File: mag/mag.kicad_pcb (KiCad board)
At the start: 4 copper layers, 68 x 41 mm, 67 parts, among them K1 кнопка_FSMSM, K2 кнопка_FSMSM, K3 кнопка_FSMSM, X1 Клеммник_х2

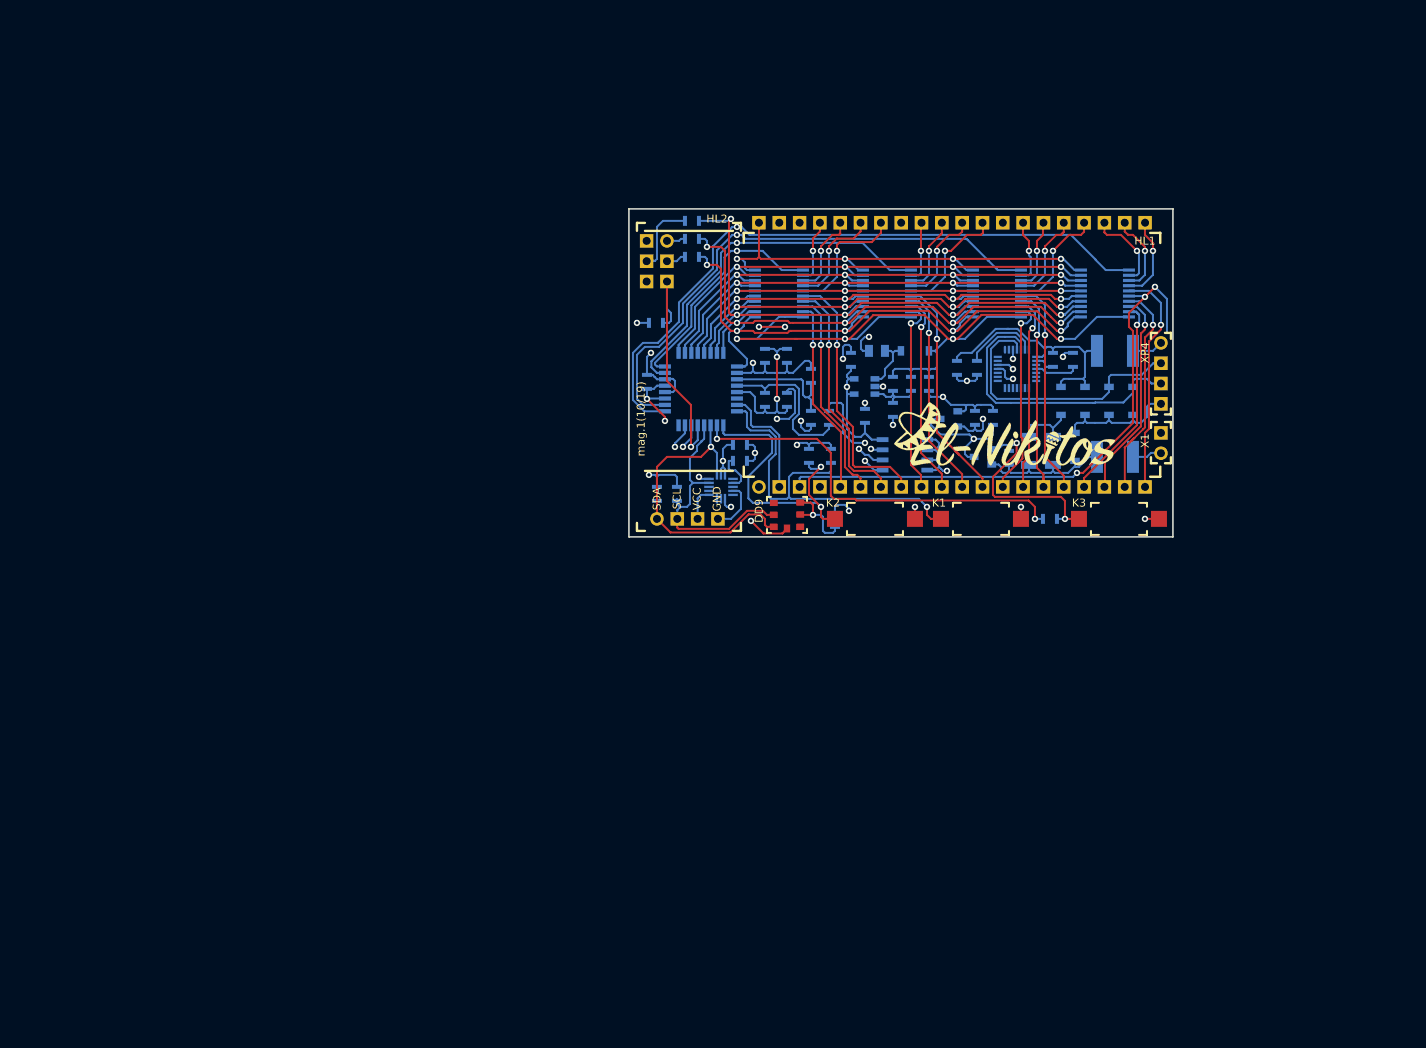
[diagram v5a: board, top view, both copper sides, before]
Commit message: инициирован переезд на ESP32
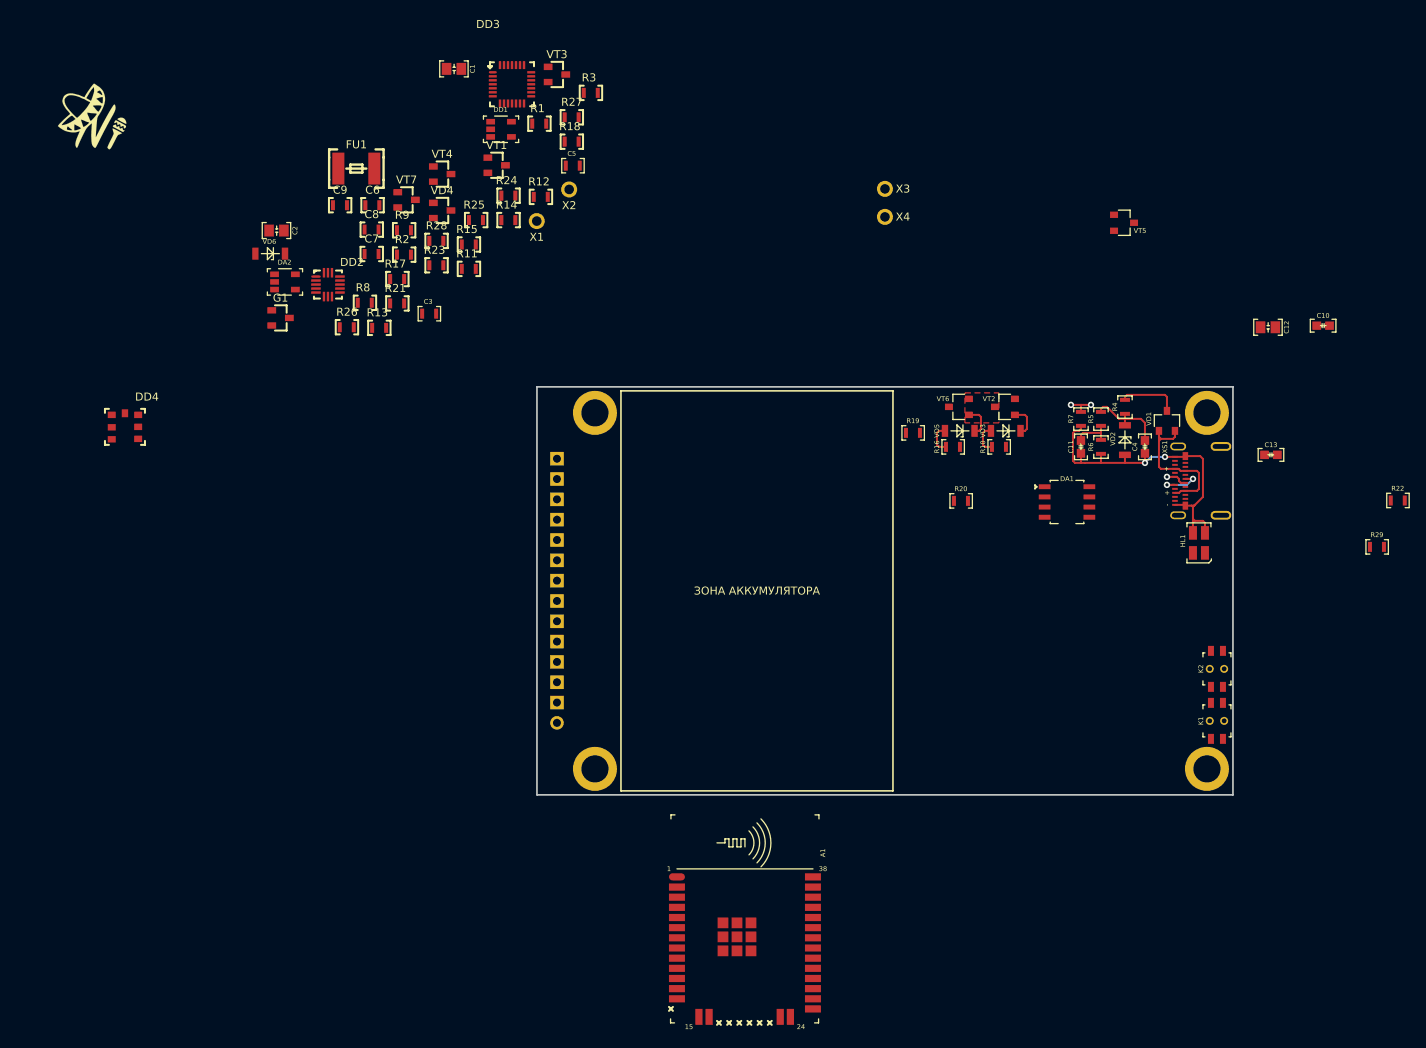
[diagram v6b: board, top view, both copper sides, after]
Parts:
- removed C14, C15: Конденсатор_керамический, N_RLC:Конденсатор_SMD_0603
- removed DD5: D-triger_74VHC573MTC, N_DD:SSOP-20
- removed DD6: LIS3DH, N_DD:акселерометр_LIS3DH
- removed DD7: Память_eeprom_AT24C512C, N_DD:SO-8
- removed DD8: Преобразователь_CP2102(USB-UART), N_DD:Микросхема_CP2102
- removed DD9: Датчик_bmp180, N_DD:BMP180
- removed FU2: Предохранитель_MF-MSMF010, N_RLC:Предохранитель_SMD_1812
- removed G***: LOGO, N_ICO:el-nikitos_29x10
- removed G***: LOGO, N_ICO:instagram_3x3
- removed G***: LOGO, N_ICO:skyer_19x4
- removed G2: Микросхема_DCDC_step_UP_TPS61040, N_G:Преобразователь_LM2703_SOT-23-5
- removed K3: кнопка_FSMSM, N_X:Кнопка_FSMSM
- removed L1: Чип-индуктивность, N_RLC:Чип-индуктивность_SMD_0805
- removed XP3: Вилка_PLD6_ПРОГ, N_X:Вилка_PLD6_вертикальная
- removed XP4: USB_female, N_X:Вилка_PLS4_вертикальная
- added A1: модуль_esp32_wroom_32_SMD_noSD, N_A:ESP32_WROOM32_pnp_noSD, F.Cu at (116.0, 132.8)
- added D1: LOGO, N_ICO:ni_10x10, F.Cu at (35.0, 29.2)
- added DA1: ОУ_LM358DT, MOTOR_IMPORT_OTK:SO-8, F.Cu at (153.5, 75.0)
- added DA2: ОУ_LMV321ILT, N_G:SOT-23-5_pnp, F.Cu at (58.5, 49.4)
- added R21: Резистор_0,065Вт, N_RLC:Резистор_SMD_0603_0,065_Вт, F.Cu at (72.5, 52.1)
- added R22: Резистор*1кОм*0603, N_RLC:Резистор_SMD_0603_0,065_Вт_pnp, F.Cu at (197.6, 76.7)
- added R23: Резистор_0,065Вт, N_RLC:Резистор_SMD_0603_0,065_Вт, F.Cu at (77.4, 47.3)
- added R24: Резистор_0,065Вт, N_RLC:Резистор_SMD_0603_0,065_Вт, F.Cu at (86.4, 38.6)
- added R25: Резистор_0,065Вт, N_RLC:Резистор_SMD_0603_0,065_Вт, F.Cu at (82.4, 41.6)
- added R26: Резистор_0,065Вт, N_RLC:Конденсатор_SMD_0603, F.Cu at (65.3, 55.0)
- added R27: Резистор_0,065Вт, N_RLC:Конденсатор_SMD_0603, F.Cu at (93.5, 28.8)
- added R28: Резистор_0,065Вт, N_RLC:Конденсатор_SMD_0603, F.Cu at (76.5, 44.2)
- added R29: Резистор*1кОм*0603, N_RLC:Резистор_SMD_0603_0,065_Вт_pnp, F.Cu at (195.0, 82.5)
- added VT2: Транзистор*pnp*0,5А*45В*SOT23, N_VD_HL:Корпус_КТ-46, F.Cu at (148.5, 65.0)
- added VT3: Транзистор_полевой_P-канал(IRLML2246TRPBF), N_VD_HL:Транзистор_IRLML6344TR_SOT-23, F.Cu at (92.5, 23.4)
- added VT4: Транзистор_полевой_N-IRLML6344TR, N_VD_HL:Транзистор_IRLML6344TR_SOT-23, F.Cu at (78.2, 35.9)
- added VT5: Транзистор*npn*0,5А*45В*SOT23, N_VD_HL:Корпус_КТ-46, F.Cu at (163.4, 42.0)
- added VT6: Транзистор*pnp*0,5А*45В*SOT23, N_VD_HL:Корпус_КТ-46, F.Cu at (142.8, 65.0)
- added VT7: Транзистор_полевой_P-канал(IRLML2246TRPBF), N_VD_HL:Транзистор_IRLML6344TR_SOT-23, F.Cu at (73.7, 39.1)
- added X2: отверстие_под_пайку, N_X:ОтверстиеD1.2, F.Cu at (94.0, 37.8)
- added X3: отверстие_под_пайку, N_X:ОтверстиеD1.2, F.Cu at (133.5, 37.8)
- added X4: отверстие_под_пайку, N_X:ОтверстиеD1.2, F.Cu at (133.5, 41.2)
- added XS1: UBS-type-C-105450-0101&упрощенная, N_X:usb-type-c, F.Cu at (169.8, 77.2)
- C1, C2: footprint N_RLC:Конденсатор_SMD_0603 -> N_RLC:Конденсатор_SMD_IEC_0805; moved to F.Cu
- C10, C11, C13, C4: value Конденсатор_керамический -> Конденсатор*0,1мкФ*25В*0603; footprint N_RLC:Конденсатор_SMD_0603 -> N_RLC:Конденсатор_SMD_IEC_0603; moved to F.Cu
- C12: value Конденсатор_керамический -> Конденсатор*10мкФ*16В*0805; footprint N_RLC:Конденсатор_SMD_0603 -> N_RLC:Конденсатор_SMD_IEC_0805; moved to F.Cu
- C3, C5: footprint N_RLC:Конденсатор_SMD_0603 -> N_RLC:Конденсатор_SMD_0603_pnp; moved to F.Cu
- C6, C7, C8, C9, VT1: moved to F.Cu
- DD1: value ATmega328 -> Микросхема_заряда_MCP73831T-2ACI_OT; footprint N_DD:микросхема_ATMEGA-8-161AU -> N_G:SOT-23-5_pnp; moved to F.Cu
- DD2: value D-triger_74VHC573MTC -> LIS3DH; footprint N_DD:SSOP-20 -> N_DD:акселерометр_LIS3DH; moved to F.Cu
- DD3: value D-triger_74VHC573MTC -> Преобразователь_CP2102(USB-UART); footprint N_DD:SSOP-20 -> N_DD:Микросхема_CP2102; moved to F.Cu
- DD4: value D-triger_74VHC573MTC -> Датчик_bmp180; footprint N_DD:SSOP-20 -> N_DD:BMP180; moved to F.Cu
- FU1: value Предохранитель_MF-MSMF010 -> Предохранитель_MF-MSMF030; moved to F.Cu
- G1: value стабилизатор_XC6206P302MR -> ИОП_LM4040BIM3-2.5_NOPB; moved to F.Cu
- HL1: value display_EDS803_EDS805 -> Светодиод_сдвоенный_KPB-3025SURKCGKC; footprint N_VD_HL:display_EDS803_805 -> N_VD_HL:Светодиод_SMD_m3025
- HL2: value oled_0.91_128x32 -> TFT-дисплей_ST7735_ILI9341; footprint N_VD_HL:oled_0.91_128x32 -> N_VD_HL:TFT_2.8_INCH; moved to B.Cu
- K1, K2: value кнопка_FSMSM -> Кнопка_KLS7-TS5401-1.35-250-T; footprint N_X:Кнопка_FSMSM -> N_X:Кнопка_KLS7-TS5401
- R1, R11, R12, R13, R14, R15, R17, R18, R2, R3, R8, R9: footprint N_RLC:Конденсатор_SMD_0603 -> N_RLC:Резистор_SMD_0603_0,065_Вт; moved to F.Cu
- R10, R16, R4: value Резистор_0,065Вт -> Резистор*1кОм*0603; footprint N_RLC:Конденсатор_SMD_0603 -> N_RLC:Резистор_SMD_0603_0,065_Вт_pnp; moved to F.Cu
- R19: value Резистор_0,065Вт -> Резистор*2,4кОм*0603; footprint N_RLC:Конденсатор_SMD_0603 -> N_RLC:Резистор_SMD_0603_0,065_Вт_pnp; moved to F.Cu
- R20, R5: value Резистор_0,065Вт -> Резистор*10кОм*0603; footprint N_RLC:Конденсатор_SMD_0603 -> N_RLC:Резистор_SMD_0603_0,065_Вт_pnp; moved to F.Cu
- R6: value Резистор_0,25Вт -> Резистор*1кОм*0603; footprint N_RLC:Резистор_SMD_1206-0,25_Вт -> N_RLC:Резистор_SMD_0603_0,065_Вт_pnp; moved to F.Cu
- R7: value Резистор_0,25Вт -> Резистор*1Ом*0603; footprint N_RLC:Резистор_SMD_1206-0,25_Вт -> N_RLC:Резистор_SMD_0603_0,065_Вт_pnp; moved to F.Cu
- VD1: value Диод_S13 -> Набор_диодов_2Д803АС9; footprint N_VD_HL:Диод_S13_SOD-123 -> MOTOR_VD_VT_HL:Корпус_КТ-46; moved to F.Cu
- VD2, VD3, VD5: value Диод_S13 -> Стабилитрон*3,3В*SOD80; footprint N_VD_HL:Диод_S13_SOD-123 -> N_VD_HL:SOD-80; moved to F.Cu
- VD4: value Диод_S13 -> Диоды_шоттки_BAR43CFILM; footprint N_VD_HL:Диод_S13_SOD-123 -> N_VD_HL:Транзистор_IRLML6344TR_SOT-23; moved to F.Cu
- VD6: value Диод_S13 -> Стабилитрон_BZV55-C3V9; footprint N_VD_HL:Диод_S13_SOD-123 -> N_VD_HL:SOD-80; moved to F.Cu
- X1: value Клеммник_х2 -> отверстие_под_пайку; footprint N_X:Вилка_PLS2_вертикальная -> N_X:ОтверстиеD1.2
- moved DD4 106.7 mm to (38.5, 66.0)
- moved FU1 105.7 mm to (65.2, 35.2), turned to 0 degrees
- moved C9 84.8 mm to (64.5, 39.8), turned to 0 degrees
- moved G1 84.5 mm to (58.0, 53.9), turned to 0 degrees
- moved VD4 84.4 mm to (78.2, 40.5), turned to 0 degrees
- moved VD6 83.3 mm to (54.8, 45.8)
- moved X1 83.2 mm to (90.0, 41.8), turned to 0 degrees
- moved C7 81.4 mm to (68.5, 45.9), turned to 0 degrees
- moved R13 80.6 mm to (70.3, 55.1), turned to 0 degrees
- moved R14 78.1 mm to (86.4, 41.6), turned to 0 degrees
- moved R11 76.3 mm to (81.5, 47.8), turned to 0 degrees
- moved VT1 70.9 mm to (85.0, 34.8), turned to 0 degrees
- moved C8 70.7 mm to (68.5, 42.8), turned to 0 degrees
- moved C13 67.3 mm to (181.8, 71.0)
- moved R8 66.7 mm to (68.5, 52.0), turned to 0 degrees
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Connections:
- C1 pad 1: /VCC_bat -> /U.PROTECT
- C1 pad 2: /gnd -> GND
- C10 pad 1: /5V -> 5V
- C10 pad 2: /gnd -> /GND-IN
- C11 pad 1: /USBtoUART/USB_pwr -> /REF-0V1
- C11 pad 2: /gnd -> /GND-IN
- C12 pad 2: /gnd -> Net-(C12-Pad2)
- C13 pad 1: /3V -> /VOL-SENS
- C13 pad 2: /gnd -> /GND-IN
- C2 pad 1: /VCC_bat -> /BAT.CHARGE
- C2 pad 2: /gnd -> GND
- C3 pad 1: /VCC_bat -> /BAT.LOAD
- C3 pad 2: /gnd -> GND
- C4 pad 1: /VCC_bat -> /REF-3V3
- C4 pad 2: /gnd -> /GND-IN
- C5 pad 1: /AREF -> 3V3
- C5 pad 2: /gnd -> GND
- C6 pad 1: /VCC_bat -> /USB_pwr
- C6 pad 2: /gnd -> /USB_pwr_gnd
- C7 pad 1: /VCC_bat -> Net-(C7-Pad1)
- C7 pad 2: /gnd -> /USB_pwr_gnd
- C8 pad 1: /5V -> /3V
- C8 pad 2: Net-(C8-Pad2) -> /USB_pwr_gnd
- C9 pad 2: /gnd -> /USB_pwr_gnd
- DD1 pad 1: /PD3 -> Net-(DD1-Pad1)
- DD1 pad 2: /PD4 -> GND
- DD1 pad 3: /gnd -> /BAT.CHARGE
- DD1 pad 4: /VCC_bat -> /U.PROTECT
- DD1 pad 5: /gnd -> Net-(DD1-Pad5)
- DD2 pad 1: /PB5_SCK -> /3V
- DD2 pad 10: /gnd -> Net-(DD2-Pad10)
- DD2 pad 11: /PB7 -> Net-(DD2-Pad11)
- DD2 pad 12: /Out18 -> /USB_pwr_gnd
- DD2 pad 13: /Out17 -> Net-(DD2-Pad13)
- DD2 pad 14: /Out16 -> /3V
- DD2 pad 15: /Out15 -> Net-(DD2-Pad15)
- DD2 pad 16: /Out14 -> Net-(DD2-Pad16)
- DD2 pad 2: /PB4_MISO -> Net-(DD2-Pad2)
- DD2 pad 3: /PB3_MOSI -> Net-(DD2-Pad3)
- DD2 pad 4: /PB2 -> /I2C_SCL
- DD2 pad 5: /PB1 -> /USB_pwr_gnd
- DD2 pad 6: /PB0 -> /I2C_SDA
- DD2 pad 7: /PD7 -> /3V
- DD2 pad 8: /PD6 -> /3V
- DD2 pad 9: /PD5 -> Net-(DD2-Pad9)
- DD3 pad 1: /PB5_SCK -> Net-(DD3-Pad1)
- DD3 pad 10: /gnd -> Net-(DD3-Pad10)
- DD3 pad 11: /PB6 -> Net-(DD3-Pad11)
- DD3 pad 12: /Out28 -> Net-(DD3-Pad12)
- DD3 pad 13: /Out27 -> Net-(DD3-Pad13)
- DD3 pad 14: /Out26 -> Net-(DD3-Pad14)
- DD3 pad 15: /Out25 -> Net-(DD3-Pad15)
- DD3 pad 16: /Out24 -> Net-(DD3-Pad16)
- DD3 pad 17: /Out23 -> Net-(DD3-Pad17)
- DD3 pad 18: /Out22 -> Net-(DD3-Pad18)
- DD3 pad 19: /Out21 -> Net-(DD3-Pad19)
- DD3 pad 2: /PB4_MISO -> Net-(DD3-Pad2)
- DD3 pad 20: /5V -> Net-(DD3-Pad20)
- DD3 pad 3: /PB3_MOSI -> /USB_pwr_gnd
- DD3 pad 4: /PB2 -> /USB_D+
- DD3 pad 5: /PB1 -> /USB_D-
- DD3 pad 6: /PB0 -> Net-(C7-Pad1)
- DD3 pad 7: /PD7 -> /USB_pwr
- DD3 pad 8: /PD6 -> /USB_pwr
- DD3 pad 9: /PD5 -> Net-(DD3-Pad9)
- DD4 pad 1: /PB5_SCK -> Net-(DD4-Pad1)
- DD4 pad 2: /PB4_MISO -> /3V
- DD4 pad 3: /PB3_MOSI -> /3V
- DD4 pad 4: /PB2 -> Net-(DD4-Pad4)
- DD4 pad 5: /PB1 -> /I2C_SCL
- DD4 pad 6: /PB0 -> /I2C_SDA
- DD4 pad 7: /PD7 -> /USB_pwr_gnd
- FU1 pad 1: /power/Battery+ -> /BAT.IN
- FU1 pad 2: /power/Bat_in+ -> /BAT.CHARGE
- G1 pad 1: /gnd -> /AN.2V5.REF
- G1 pad 2: /3V -> GND
- G1 pad 3: /VCC_bat -> Net-(G1-Pad3)
- HL1 pad 1: /gnd -> Net-(HL1-Pad1)
- HL1 pad 2: /PC0 -> /GND-IN
- HL1 pad 3: /Out44 -> Net-(HL1-Pad3)
- HL1 pad 4: Net-(HL1-Pad4) -> /GND-IN
- HL2 pad 1: /SDA -> 3V3
- HL2 pad 2: /SCL -> GND
- HL2 pad 3: /3V -> /TFT-CS
- HL2 pad 4: /gnd -> /TFT-RES
- K1 pad 1: /PC1 -> Net-(K1-Pad1)
- K1 pad 2: /gnd -> Net-(K1-Pad1)
- K2 pad 1: /PC2 -> /BOOT
- K2 pad 2: /gnd -> /BOOT
- R1 pad 1: /VCC_bat -> Net-(R1-Pad1)
- R1 pad 2: /SDA -> GND
- R10 pad 1: /USBtoUART/USB_pwr -> Net-(R10-Pad1)
- R10 pad 2: Net-(DD8-Pad9) -> /CUR-DIRECT
- R11 pad 1: /gnd -> Net-(K1-Pad1)
- R11 pad 2: Net-(DD8-Pad11) -> 3V3
- R12 pad 1: Net-(DD6-Pad10) -> /BAT.CHARGE
- R12 pad 2: /gnd -> Net-(R12-Pad2)
- R13 pad 1: /power/Bat_in+ -> Net-(R13-Pad1)
- R13 pad 2: Net-(K3-Pad1) -> GND
- R14 pad 1: Net-(K3-Pad1) -> /SELF.TURN
- R14 pad 2: /PC3 -> Net-(R13-Pad1)
- R15 pad 1: /VCC_bat -> /BUTT.TURN
- R15 pad 2: /PC1 -> /EXT.BUTT
- R16 pad 1: /VCC_bat -> Net-(R16-Pad1)
- R16 pad 2: /PC2 -> /VOL-DIRECT
- R17 pad 1: /AREF -> /BAT.LOAD
- R17 pad 2: /3V -> /AN.BAT.MEASURE
- R18 pad 1: /PB4_MISO -> /AN.BAT.MEASURE
- R18 pad 2: Net-(R18-Pad2) -> GND
- R19 pad 1: /PB5_SCK -> /max4V1
- R19 pad 2: Net-(R19-Pad2) -> /VOL-SENS
- R2 pad 1: /VCC_bat -> /U.PROTECT
- R2 pad 2: /SCL -> Net-(R1-Pad1)
- R20 pad 1: /PB3_MOSI -> /VOL-SENS
- R20 pad 2: Net-(R20-Pad2) -> /GND-IN
- R3 pad 1: /VCC_bat -> Net-(DD1-Pad5)
- R3 pad 2: /RES -> GND
- R4 pad 1: /VCC_bat -> 5V
- R4 pad 2: /ADC6 -> /REF-3V3
- R5 pad 1: /ADC6 -> /REF-3V3
- R5 pad 2: /gnd -> /REF-0V1
- R6 pad 1: /power/Bat_in+ -> /REF-0V1
- R6 pad 2: Net-(R6-Pad2) -> /GND-IN
- R7 pad 1: /power/Bat_in+ -> GND
- R7 pad 2: Net-(R6-Pad2) -> /GND-IN
- R8 pad 1: /5V -> /CHARGE.MODE
- R8 pad 2: Net-(C8-Pad2) -> Net-(DD1-Pad1)
- R9 pad 1: Net-(C8-Pad2) -> Net-(K1-Pad1)
- R9 pad 2: /gnd -> /RESET
- VD1 pad 1: /gnd -> /UIN
- VD1 pad 2: /USBtoUART/USB_pwr -> /UIN
- VD2 pad 1: /gnd -> /GND-IN
- VD2 pad 2: /USB_D- -> /REF-3V3
- VD3 pad 1: /gnd -> Net-(R10-Pad1)
- VD3 pad 2: /USB_D+ -> Net-(VD3-Pad2)
- VD4 pad 1: /gnd -> Net-(R12-Pad2)
- VD4 pad 2: /power/Bat_in+ -> Net-(R12-Pad2)
- VD5 pad 1: /USBtoUART/USB_pwr -> Net-(R16-Pad1)
- VD5 pad 2: Net-(R6-Pad2) -> Net-(VD5-Pad2)
- VD6 pad 1: Net-(G2-Pad1) -> GND
- VD6 pad 2: /5V -> 3V3
- VT1 pad 1: Net-(K3-Pad1) -> Net-(R1-Pad1)
- VT1 pad 2: /power/Bat_in+ -> /U.PROTECT
- VT1 pad 3: /VCC_bat -> /U.IN
- X1 pad 1: /power/Battery+ -> GND
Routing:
- net /gnd: track 169.1 -> 0.00 mm, vias 26 -> 0
- net /5V: track 97.3 -> 0.00 mm, vias 4 -> 0
- net /SDA: track 84.4 -> 0.00 mm, vias 2 -> 0
- net /PD3: track 84.0 -> 0.00 mm, vias 1 -> 0
- net /PB5_SCK: track 79.6 -> 0.00 mm, vias 5 -> 0
- net /PB3_MOSI: track 79.4 -> 0.00 mm, vias 5 -> 0
- net /VCC_bat: track 79.3 -> 0.00 mm, vias 9 -> 0
- net /PB4_MISO: track 77.5 -> 0.00 mm, vias 5 -> 0
- net /Out44: track 74.0 -> 0.00 mm, vias 3 -> 0
- net /SCL: track 71.1 -> 0.00 mm, vias 1 -> 0
- net /PD4: track 68.1 -> 0.00 mm, vias 1 -> 0
- net /PD5: track 65.3 -> 0.00 mm, vias 4 -> 0
- net /PD6: track 63.4 -> 0.00 mm, vias 4 -> 0
- net /PB2: track 62.3 -> 0.00 mm, vias 4 -> 0
- net /PD7: track 61.5 -> 0.00 mm, vias 4 -> 0
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- added copper zone on F.Cu, net /max0.3A
- added copper zone on In2.Cu, net 3V3
- added copper zone on In1.Cu, net GND
- removed copper zone on In2.Cu, net /3V
- removed copper zone on In2.Cu, net /VCC_bat
- removed copper zone on In1.Cu, net /gnd
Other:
- board size 68 x 41 mm -> 87 x 51 mm
- board text added: "ЗОНА АККУМУЛЯТОРА"
- board text added: "ЗОНА ДИСПЛЕЯ"
- board text removed: "GND"
- board text removed: "R"
- board text removed: "SCL"
- board text removed: "SDA"
- board text removed: "VCC"
- board text removed: "el.a.nikitos"
- board text removed: "mag.1(10/19)"

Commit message: подготовлена схема заряда АБ, начата схема питания МК
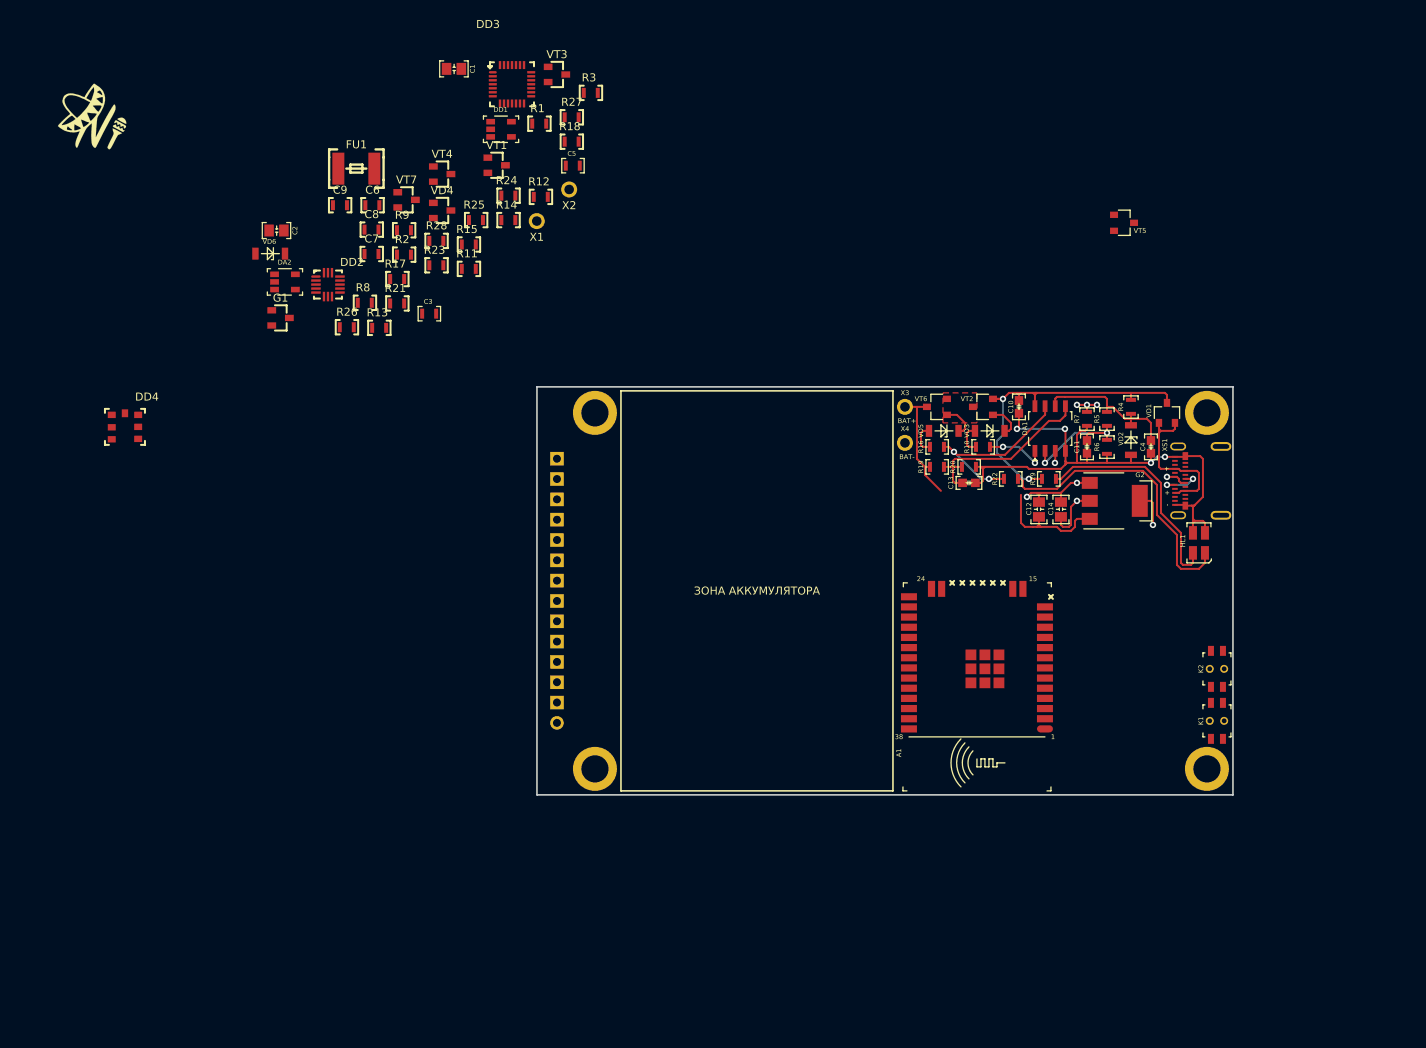
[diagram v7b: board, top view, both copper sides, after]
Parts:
- added C14: Конденсатор*10мкФ*16В*0805, N_RLC:Конденсатор_SMD_IEC_0805, F.Cu at (155.5, 78.8)
- added G2: Микросхема*LDO*IN8V*OUT3V3*1,2A*SOT-223, N_VD_HL:Транзистор_NPN_SOT223_pnp, F.Cu at (162.2, 76.8)
- moved R22 48.4 mm to (149.2, 74.0), turned to 180 degrees
- moved A1 46.6 mm to (145.0, 96.2), turned to 180 degrees
- moved R29 41.9 mm to (154.0, 74.0), turned to 180 degrees
- moved C10 39.4 mm to (150.2, 65.0), turned to 270 degrees
- moved C13 37.9 mm to (144.0, 74.5)
- moved C12 36.5 mm to (152.8, 78.8), turned to 90 degrees
- moved X4 28.4 mm to (136.0, 69.5)
- moved X3 27.4 mm to (136.0, 65.0)
- moved R19 5.20 mm to (140.0, 72.5)
- moved DA1 4.70 mm to (152.3, 70.5), turned to 0 degrees
- moved R20 4.37 mm to (144.0, 72.5)
- moved VT2 2.75 mm to (145.8, 65.0)
- moved VT6 2.75 mm to (140.0, 65.0)
- moved R10 2.00 mm to (145.8, 70.0)
- moved R16 2.00 mm to (140.0, 70.0)
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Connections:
- C12 pad 2: Net-(C12-Pad2) -> GND
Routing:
- net Net-(HL1-Pad1): track 0.00 -> 36.3 mm
- net 5V: track 7.58 -> 43.2 mm, vias 0 -> 2
- net /GND-IN: track 42.4 -> 71.6 mm, vias 2 -> 4
- net Net-(HL1-Pad3): track 0.00 -> 28.6 mm
- net /VOL-DIRECT: track 0.00 -> 23.9 mm, vias 0 -> 2
- net /VOL-SENS: track 0.00 -> 23.4 mm
- net Net-(C12-Pad1): track 0.00 -> 15.3 mm
- net /max4V1: track 0.00 -> 15.1 mm
- net GND: track 3.38 -> 16.0 mm, vias 2 -> 6
- net 3V3: track 0.00 -> 11.9 mm, vias 0 -> 2
- net /REF-0V1: track 4.80 -> 15.6 mm, vias 0 -> 2
- net /REF-3V3: track 10.4 -> 19.2 mm
- net /CUR-DIRECT: track 0.00 -> 8.20 mm, vias 0 -> 2
- net /UIN: track 18.3 -> 19.3 mm
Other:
- board text added: "BAT+"
- board text added: "BAT-"

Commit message: подготовлена схема включения 3,3В, не установлен источник 2,5В
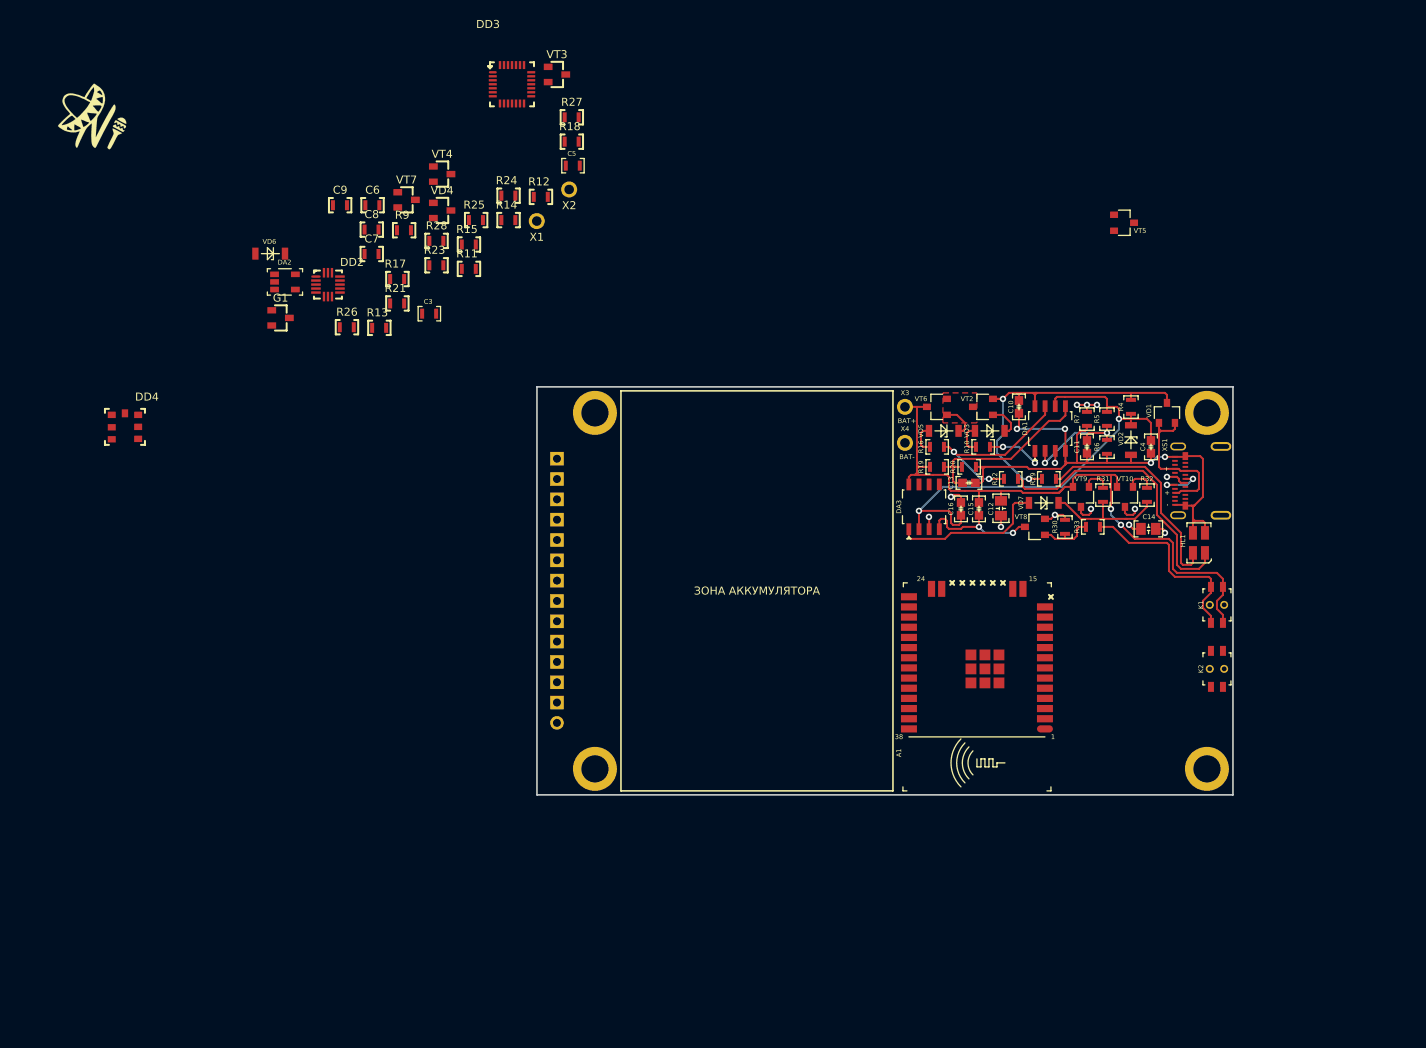
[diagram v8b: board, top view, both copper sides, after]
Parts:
- removed C1, C2: Конденсатор_керамический, N_RLC:Конденсатор_SMD_IEC_0805
- removed DD1: Микросхема_заряда_MCP73831T-2ACI_OT, N_G:SOT-23-5_pnp
- removed FU1: Предохранитель_MF-MSMF030, N_RLC:Предохранитель_SMD_1812
- removed G2: Микросхема*LDO*IN8V*OUT3V3*1,2A*SOT-223, N_VD_HL:Транзистор_NPN_SOT223_pnp
- removed R1, R2, R3, R8: Резистор_0,065Вт, N_RLC:Резистор_SMD_0603_0,065_Вт
- removed VT1: Транзистор_полевой_P-канал(IRLML2246TRPBF), N_VD_HL:Транзистор_IRLML6344TR_SOT-23
- added C15: Конденсатор*0,1мкФ*25В*0603, N_RLC:Конденсатор_SMD_IEC_0603, F.Cu at (145.2, 77.8)
- added C16: Конденсатор*0,1мкФ*25В*0603, N_RLC:Конденсатор_SMD_IEC_0603, F.Cu at (143.0, 77.8)
- added DA3: ОУ_LM358DT, MOTOR_IMPORT_OTK:SO-8, F.Cu at (136.5, 80.2)
- added R30: Резистор*10кОм*0603, N_RLC:Резистор_SMD_0603_0,065_Вт_pnp, F.Cu at (156.0, 80.0)
- added R31: Резистор*1кОм*0603, N_RLC:Резистор_SMD_0603_0,065_Вт_pnp, F.Cu at (160.8, 76.0)
- added R32: Резистор*1кОм*0603, N_RLC:Резистор_SMD_0603_0,065_Вт_pnp, F.Cu at (166.2, 76.0)
- added R33: Резистор*1кОм*0603, N_RLC:Резистор_SMD_0603_0,065_Вт_pnp, F.Cu at (159.5, 80.0)
- added VD7: Стабилитрон*3,3В*SOD80, N_VD_HL:SOD-80, F.Cu at (151.5, 77.0)
- added VT10: Транзистор*pnp*0,5А*45В*SOT23, N_VD_HL:Корпус_КТ-46, F.Cu at (163.5, 76.2)
- added VT8: Транзистор_полевой_N-канальный_КП526А9, MOTOR_VD_VT_HL:Корпус_КТ-46, F.Cu at (152.2, 80.0)
- added VT9: Транзистор*pnp*0,5А*45В*SOT23, N_VD_HL:Корпус_КТ-46, F.Cu at (158.0, 76.2)
- moved K1 14.5 mm to (175.8, 92.0)
- moved C14 10.1 mm to (165.5, 80.2), turned to 0 degrees
- moved C12 5.15 mm to (148.0, 76.8), turned to 270 degrees
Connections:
- net /BAT.CHARGE renamed Net-(R12-Pad1)
- C12 pad 1: Net-(C12-Pad1) -> /max4V1
- K1 pad 3: GND -> /max4V1
- K1 pad 4: GND -> /max4V1
- R11 pad 1: Net-(K1-Pad1) -> Net-(R11-Pad1)
- R9 pad 1: Net-(K1-Pad1) -> Net-(R11-Pad1)
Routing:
- net /max4V1: track 15.1 -> 80.0 mm, vias 0 -> 2
- net /REF-3V3: track 19.2 -> 60.5 mm, vias 0 -> 2
- net Net-(K1-Pad1): track 0.00 -> 24.8 mm
- net /LDO-DIRECT: track 0.00 -> 19.3 mm
- net Net-(R31-Pad2): track 0.00 -> 15.5 mm
- net Net-(C12-Pad1): track 15.3 -> 0.00 mm
- net /COM: track 0.00 -> 15.0 mm, vias 0 -> 2
- net Net-(R30-Pad2): track 0.00 -> 7.08 mm
- net Net-(R32-Pad1): track 0.00 -> 3.58 mm
- net Net-(R31-Pad1): track 0.00 -> 3.58 mm
- net 3V3: track 11.9 -> 8.66 mm, vias 2 -> 4
- net GND: track 16.0 -> 13.1 mm, vias 6 -> 8
